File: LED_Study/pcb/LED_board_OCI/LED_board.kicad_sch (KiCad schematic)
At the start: 4 parts

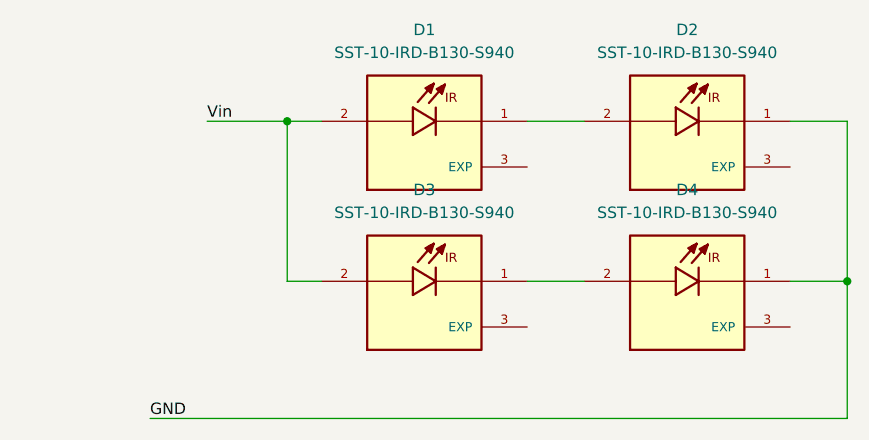
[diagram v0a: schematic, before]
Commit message: updated boards and ordered from PCBway
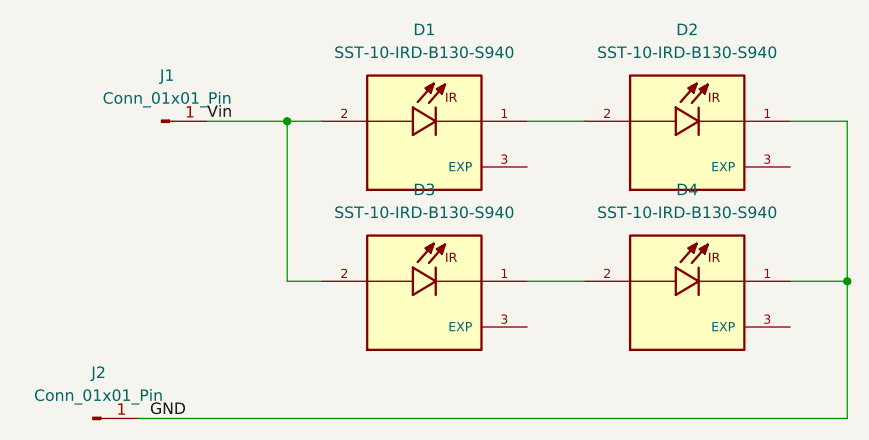
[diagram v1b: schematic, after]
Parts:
- added J1, J2: Conn_01x01_Pin, Connector_PinHeader_1.00mm:PinHeader_1x01_P1.00mm_Vertical, symbol Connector:Conn_01x01_Pin
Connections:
- net GND: now also J2.1 (Pin_1)
- net Vin: now also J1.1 (Pin_1)
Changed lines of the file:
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@@
     (stroke (width 0) (type default))
   )
-  (wire (pts (xy 68.58 72.39) (xy 146.05 72.39))
+  (wire (pts (xy 67.31 72.39) (xy 146.05 72.39))
     (stroke (width 0) (type default))
   )
@@
         )
       )
+    )
+  )
+  (symbol (lib_id "Connector:Conn_01x01_Pin") (at 69.85 39.37 0) (unit 1)
+    (in_bom yes) (on_board yes) (dnp no) (fields_autoplaced)
+    (property "Reference" "J1" (at 70.485 34.29 0)
+      (effects (font (size 1.27 1.27)))
+    )
+    (property "Value" "Conn_01x01_Pin" (at 70.485 36.83 0)
+      (effects (font (size 1.27 1.27)))
+    )
+    (property "Footprint" "Connector_PinHeader_1.00mm:PinHeader_1x01_P1.00mm_Vertical" (at 69.85 39.37 0)
+      (effects (font (size 1.27 1.27)) hide)
+    )
+    (property "Datasheet" "~" (at 69.85 39.37 0)
+      (effects (font (size 1.27 1.27)) hide)
+    )
+    (pin "1")
+    (instances
+      (project "LED_board"
+        (path "/ee3210f4-4163-4542-8403-a0d7023a83cd"
+          (reference "J1") (unit 1)
+        )
+      )
+    )
+  )
+  (symbol (lib_id "Connector:Conn_01x01_Pin") (at 62.23 72.39 0) (unit 1)
+    (in_bom yes) (on_board yes) (dnp no) (fields_autoplaced)
+    (property "Reference" "J2" (at 62.865 67.31 0)
+      (effects (font (size 1.27 1.27)))
+    )
+    (property "Value" "Conn_01x01_Pin" (at 62.865 69.85 0)
+      (effects (font (size 1.27 1.27)))
+    )
+    (property "Footprint" "Connector_PinHeader_1.00mm:PinHeader_1x01_P1.00mm_Vertical" (at 62.23 72.39 0)
+      (effects (font (size 1.27 1.27)) hide)
+    )
+    (property "Datasheet" "~" (at 62.23 72.39 0)
+      (effects (font (size 1.27 1.27)) hide)
+    )
+    (pin "1")
+    (instances
+      (project "LED_board"
+        (path "/ee3210f4-4163-4542-8403-a0d7023a83cd"
+          (reference "J2") (unit 1)
+        )
+      )
